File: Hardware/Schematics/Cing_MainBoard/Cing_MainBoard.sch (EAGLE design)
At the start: 116 parts, among them IC1 L293D, IC3 FT232RL, Q1 16mhz, Q2 BSS138, Q3 BSS138, Q4 BSS138, Q5 BSS138, U2 BMP180, U3 MPU-6050MPU6050

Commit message: commit
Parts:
- removed R8, R9: 1k, rcl:R-EU_R1206
- removed U$8: BATTERY_18650-HOLDER, Cing Library:BATTERY_18650-HOLDER
- added BT1: (no value), Cing Library:BATTERY-AA_KIT
- added IC2, IC4: Attiny85, Cing Library:TINY85-20SU
- added LED2: Empty, led:LEDSMT1206
- added M1: ELECTRET_MICROPHON-F6035AP, microphon:ELECTRET_MICROPHON-F6035AP
- added Q6: BSS138, Cing Library:BSS138
- added R42, R44, R45: 10k, rcl:R-EU_R1206
- added R43: 100, rcl:R-EU_R1206
- added SP1: AL11P, buzzer:AL11P
- added YELLOW1: Full, led:LEDSMT1206
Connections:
- removed net N$3: R8.1, U$1.D1
- removed net N$6: R9.1, U$1.D0
- new net N$21: IC2.PB1/PCINT1/AIN1/OC0B/INT0/MISO, LED2.A
- new net N$28: Q6.D, SP1.1
- new net N$30: LED2.C, R43.1, YELLOW1.C
- new net N$37: IC2.PB4/PCINT4/ADC2, YELLOW1.A
- new net N$38: IC4.PB1/PCINT1/AIN1/OC0B/INT0/MISO, Q6.G, R45.1
- new net VOLTAGE_SENSE: IC2.PB3/PCINT3/CLKI/ADC3, R42.2, R44.1
- net +3V3: now also IC2.VCC, IC4.VCC, SP1.2
- net GND: now also BT1.-, IC2.GND, IC4.GND, Q6.S, R43.2, R44.2, R45.2; no longer U$8.-, U$8.-1, U$8.-2
- net IRFU: now also BT1.+, R42.1; no longer U$8.+, U$8.+1, U$8.+2
- net RXD: now also U$1.D0; no longer R9.2
- net SCL: now also IC2.PB2/PCINT2/SCK/ADC1/T0, IC4.PB2/PCINT2/SCK/ADC1/T0
- net SDA: now also IC2.PB0/PCINT0/AIN0/OC0A/MOSI, IC4.PB0/PCINT0/AIN0/OC0A/MOSI
- net TXD: now also U$1.D1; no longer R8.2

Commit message: commit
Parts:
- added JP1: (no value), pinhead:PINHD-1X3
- added LED10, LED11, LED4, LED9: WS2812B3535, adafruit:WS2812B3535
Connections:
- new net N$41: JP1.2, LED11.DO, LED8.DO
- net +3V3: now also JP1.1, LED10.VDD, LED11.VDD, LED4.VDD, LED9.VDD
- net GND: now also JP1.3, LED10.GND, LED11.GND, LED4.GND, LED9.GND
- net N$1: now also LED10.DO, LED9.DI
- net N$11: now also LED11.DI, LED4.DO
- net N$12: now also LED10.DI
- net N$2: now also LED4.DI, LED9.DO

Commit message: commit
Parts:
- removed D2: CGRM4007-G, diode:CGRM4007-G
- removed LED2: Empty, led:LEDSMT1206
- removed R42, R44: 10k, rcl:R-EU_R1206
- removed R43: 100, rcl:R-EU_R1206
- removed U$21: DC-DC-STEP-UP-MT3608, Cing Library:DC-DC-STEP-UP-MT3608
- removed U2: BMP180, Cing Library:BMP180
- removed YELLOW1: Full, led:LEDSMT1206
- added 1, 8205: 8205, FS8205A:DMN3024LSD
- added C14, C15: 22uf, rcl:C-EUC1206
- added C16: 100n, rcl:C-EUC1206
- added C17: (no value), rcl:CPOL-EUE3.5-8
- added D3: (no value), adafruit:DIODESMA
- added IC5: BME280, bosch-bme280:BME280
- added L1: DR125, inductors:DR125
- added L2: DR127, inductors:DR127
- added R46, R47, R8: 1k, rcl:R-EU_R1206
- added R48: 100, rcl:R-EU_R1206
- added R49: 7k5, rcl:R-EU_R1206
- added R9: 12k, rcl:R-EU_R1206
- added SJ1: (no value), jumper:SJW
- added SJ2: (no value), jumper:SJ
- added U$13: ADS1015IDGT, bt_adc:ADS1015IDGT
- added U$5: MT3608SOT23-6, MT3608:MT3608SOT23-6
- added U$8: DW01, DW01:DW01
- added U$9: LM1117, Cing Library:LM1117
- D1: value CGRM4007-G -> (none); device diode:CGRM4007-G -> adafruit:DIODESMA
- IC2: value Attiny85 -> LM2576S; device Cing Library:TINY85-20SU -> lm2576:LM2576S
- R4: value 1k2 -> 1k
- R41: value 10k -> 2; device rcl:R-EU_R1206 -> rcl:R-EU_R2512
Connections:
- removed net N$23: D1.A, D2.C, R41.1, TP4056.BAT
- removed net N$30: LED2.C, R43.1, YELLOW1.C
- removed net N$37: IC2.PB4/PCINT4/ADC2, YELLOW1.A
- removed net VOLTAGE_SENSE: IC2.PB3/PCINT3/CLKI/ADC3, R42.2, R44.1
- new net BAT-: 1A.S, 8205A.S, BT1.-, C16.2, U$7.-, U$8.GND
- new net CUR-SENSE: R22.1, R41.2, SW5.CH1B, SW5.CH2B, U$13.AIN2
- new net N$3: 1A.D, 1B.D
- new net N$35: R46.1, R49.2, R9.2, U$5.FB
- new net N$44: D3.A, L1.2, U$5.SW
- new net N$46: C14.1, D3.C, R49.1, R9.1, SJ1.1
- new net N$47: 8205A.D, 8205B.D
- new net N$48: 1A.G, 8205A.G, U$8.0D
- new net N$49: 1B.G, 8205B.G, U$8.0C
- new net N$50: C16.1, R48.1, U$8.VCC
- new net N$54: R47.1, U$8.CS
- new net N$6: R4.2, R8.1
- new net VCC_SERVO: C17.+, IC2.FB, JP2.2, JP3.2, JP4.2, L2.2
- new net VDD: U$13.VDD, U$9.OUT, U$9.VO
- net +3V3: now also IC5.CSB, IC5.VDD, IC5.VDDIO; no longer IC2.VCC, U2.VDD, U2.VDDIO
- net BAT+: now also C15.1, L1.1, R41.1, R48.2, U$13.AIN0, U$13.AIN3, U$5.EN, U$5.IN, U$9.VI; no longer R22.1, SW5.CH1B, SW5.CH2B, U$21.IN+
- net GND: now also 1B.S, 8205B.S, C14.2, C15.2, C17.-, D1.A, IC5.GND, IC5.SDO, R46.2, R47.2, R8.2, U$13.ADDR, U$13.AIN1, U$13.GND, U$5.GND, U$9.GND; no longer BT1.-, D2.A, R4.2, R43.2, R44.2, U$21.IN-, U$21.OUT-, U$7.-, U2.GND
- net IRFU: now also SJ2.1; no longer D1.C, R41.2, R42.1
- net N$21: now also D1.C, IC2.OUT, L2.1; no longer IC2.PB1/PCINT1/AIN1/OC0B/INT0/MISO, LED2.A
- net N$26: now also SJ2.2, TP4056.BAT
- net SCL: now also IC5.SCK, U$13.SCL; no longer IC2.PB2/PCINT2/SCK/ADC1/T0, U2.SCL
- net SDA: now also IC5.SDI, U$13.SDA; no longer IC2.PB0/PCINT0/AIN0/OC0A/MOSI, U2.SDA
- net VCC_MOT: now also IC2.VIN, SJ1.2; no longer JP2.2, JP3.2, JP4.2, U$21.OUT+
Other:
- moved on the sheet: BT1, C10, C4, C5, C9, D1, R22, R3, SW1, SW5, TP4056, U$6

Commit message: commit
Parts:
- removed IC4: Attiny85, Cing Library:TINY85-20SU
- removed M1: ELECTRET_MICROPHON-F6035AP, microphon:ELECTRET_MICROPHON-F6035AP
- removed Q6: BSS138, Cing Library:BSS138
- removed R45: 10k, rcl:R-EU_R1206
- removed SP1: AL11P, buzzer:AL11P
- added U$14: RANGING-SENSOR-VL53L0X, diy-modules:RANGING-SENSOR-VL53L0X
- U$16: value 3.3V -> BAT+
- U$9: value LM1117 -> LM1117-5V
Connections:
- removed net N$28: Q6.D, SP1.1
- removed net N$38: IC4.PB1/PCINT1/AIN1/OC0B/INT0/MISO, Q6.G, R45.1
- net +3V3: no longer IC4.VCC, SP1.2, U$16.LEGO
- net BAT+: now also U$16.LEGO
- net GND: now also U$14.GND; no longer IC4.GND, Q6.S, R45.2
- net SCL: now also U$14.SCL; no longer IC4.PB2/PCINT2/SCK/ADC1/T0
- net SDA: now also U$14.SDA; no longer IC4.PB0/PCINT0/AIN0/OC0A/MOSI
- net VDD: now also U$14.VIN

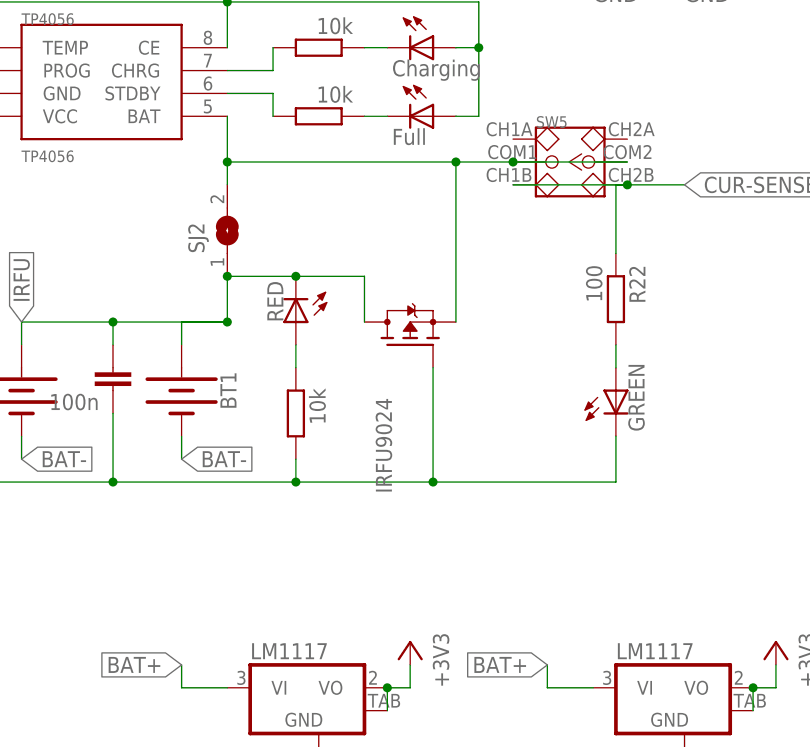
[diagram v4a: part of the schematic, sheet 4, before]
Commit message: Adding better P-fet
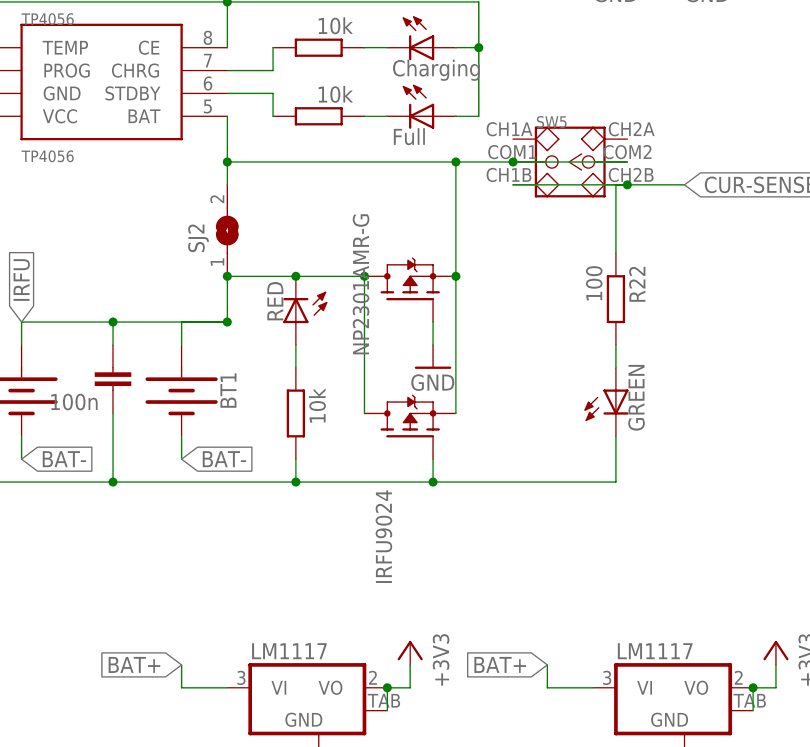
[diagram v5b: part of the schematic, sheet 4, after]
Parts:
- added Q7: NP2301AMR-G, transistor-fet:BSA223SP
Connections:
- net GND: now also Q7.G
- net IRFU: now also Q7.D
- net N$26: now also Q7.S
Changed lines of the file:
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@@
 <part name="U$14" library="diy-modules" deviceset="RANGING-SENSOR-VL53L0X" device=""/>
 <part name="GND48" library="supply1" library_urn="urn:adsk.eagle:library:371" deviceset="GND" device=""/>
+<part name="Q7" library="transistor-fet" library_urn="urn:adsk.eagle:library:396" deviceset="BSA223SP" device="" package3d_urn="urn:adsk.eagle:package:28542/1" value="NP2301AMR-G"/>
+<part name="GND49" library="supply1" library_urn="urn:adsk.eagle:library:371" deviceset="GND" device=""/>
 </parts>
 <sheets>
@@
 <attribute name="VALUE" x="251.46" y="53.34" size="1.778" layer="96" rot="MR90"/>
 </instance>
-<instance part="IRFU9024" gate="G$1" x="208.28" y="91.44" smashed="yes" rot="MR90"/>
+<instance part="IRFU9024" gate="G$1" x="208.28" y="81.28" smashed="yes" rot="MR90"/>
 <instance part="U$7" gate="G$1" x="165.1" y="86.36" smashed="yes" rot="R270"/>
 <instance part="TP4056" gate="G$1" x="165.1" y="127" smashed="yes">
@@
 <attribute name="NAME" x="63.5" y="104.14" size="1.27" layer="95" rot="R90"/>
 <attribute name="VALUE" x="69.85" y="104.14" size="1.27" layer="96" rot="R90"/>
+</instance>
+<instance part="Q7" gate="G$1" x="208.28" y="96.52" smashed="yes" rot="MR90">
+<attribute name="VALUE" x="201.93" y="90.17" size="1.778" layer="96" rot="MR90"/>
+</instance>
+<instance part="GND49" gate="1" x="210.82" y="88.9" smashed="yes">
+<attribute name="VALUE" x="208.28" y="86.36" size="1.778" layer="96"/>
 </instance>
 </instances>
@@
 <wire x1="175.26" y1="76.2" x2="195.58" y2="76.2" width="0.1524" layer="91"/>
 <wire x1="195.58" y1="76.2" x2="210.82" y2="76.2" width="0.1524" layer="91"/>
-<wire x1="210.82" y1="88.9" x2="210.82" y2="76.2" width="0.1524" layer="91"/>
+<wire x1="210.82" y1="78.74" x2="210.82" y2="76.2" width="0.1524" layer="91"/>
 <junction x="210.82" y="76.2"/>
 <pinref part="C1" gate="G$1" pin="2"/>
@@
 <junction x="66.04" y="104.14"/>
 </segment>
+<segment>
+<pinref part="Q7" gate="G$1" pin="G"/>
+<pinref part="GND49" gate="1" pin="GND"/>
+<wire x1="210.82" y1="91.44" x2="210.82" y2="93.98" width="0.1524" layer="91"/>
+</segment>
 </net>
 <net name="IRFU" class="0">
@@
 <wire x1="187.96" y1="99.06" x2="187.96" y2="93.98" width="0.1524" layer="91"/>
 <wire x1="195.58" y1="99.06" x2="187.96" y2="99.06" width="0.1524" layer="91"/>
-<wire x1="203.2" y1="93.98" x2="203.2" y2="99.06" width="0.1524" layer="91"/>
+<wire x1="203.2" y1="83.82" x2="203.2" y2="99.06" width="0.1524" layer="91"/>
 <wire x1="203.2" y1="99.06" x2="195.58" y2="99.06" width="0.1524" layer="91"/>
 <pinref part="BT1" gate="G$1" pin="+"/>
@@
 <pinref part="SJ2" gate="1" pin="1"/>
 <junction x="187.96" y="99.06"/>
+<pinref part="Q7" gate="G$1" pin="D"/>
+<junction x="203.2" y="99.06"/>
 </segment>
 </net>
@@
 <wire x1="219.71" y1="111.76" x2="213.36" y2="111.76" width="0.1524" layer="91"/>
 <junction x="219.71" y="111.76"/>
-<wire x1="213.36" y1="93.98" x2="213.36" y2="111.76" width="0.1524" layer="91"/>
+<wire x1="213.36" y1="83.82" x2="213.36" y2="99.06" width="0.1524" layer="91"/>
 <pinref part="IRFU9024" gate="G$1" pin="S"/>
 <pinref part="TP4056" gate="G$1" pin="BAT"/>
+<wire x1="213.36" y1="99.06" x2="213.36" y2="111.76" width="0.1524" layer="91"/>
 <wire x1="187.96" y1="116.84" x2="187.96" y2="111.76" width="0.1524" layer="91"/>
 <wire x1="187.96" y1="111.76" x2="213.36" y2="111.76" width="0.1524" layer="91"/>
@@
 <wire x1="187.96" y1="111.76" x2="187.96" y2="109.22" width="0.1524" layer="91"/>
 <junction x="187.96" y="111.76"/>
-</segment>
-</net>
+<pinref part="Q7" gate="G$1" pin="S"/>
+<junction x="213.36" y="99.06"/>
+</segment>
+</net>

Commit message: commit
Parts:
- added Q6: NP2301AMR-G, transistor-fet:BSA223SP
- added U$15: (no value), diy-modules:COMPASS-HMC5883L
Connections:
- net +3V3: now also U$15.VCC
- net GND: now also Q6.G, U$15.GND
- net IRFU: now also Q6.D
- net N$26: now also Q6.S
- net SCL: now also U$15.SCL
- net SDA: now also U$15.SDA

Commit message: commit
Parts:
- renumbered JP1 to WS2812
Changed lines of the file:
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@@
 <part name="GND52" library="supply1" library_urn="urn:adsk.eagle:library:371" deviceset="GND" device=""/>
 <part name="GND53" library="supply1" library_urn="urn:adsk.eagle:library:371" deviceset="GND" device=""/>
-<part name="JP1" library="pinhead" library_urn="urn:adsk.eagle:library:325" deviceset="PINHD-1X3" device="" package3d_urn="urn:adsk.eagle:package:22458/2"/>
+<part name="WS2812" library="pinhead" library_urn="urn:adsk.eagle:library:325" deviceset="PINHD-1X3" device="" package3d_urn="urn:adsk.eagle:package:22458/2"/>
 <part name="GND54" library="supply1" library_urn="urn:adsk.eagle:library:371" deviceset="GND" device=""/>
 <part name="+3V27" library="supply1" library_urn="urn:adsk.eagle:library:371" deviceset="+3V3" device=""/>
@@
 <attribute name="VALUE" x="43.18" y="96.52" size="1.778" layer="96" rot="MR180"/>
 </instance>
-<instance part="JP1" gate="A" x="142.24" y="66.04" smashed="yes">
+<instance part="WS2812" gate="A" x="142.24" y="66.04" smashed="yes">
 <attribute name="NAME" x="143.51" y="71.755" size="1.778" layer="95"/>
 <attribute name="VALUE" x="135.89" y="58.42" size="1.778" layer="96"/>
@@
 </segment>
 <segment>
-<pinref part="JP1" gate="A" pin="3"/>
+<pinref part="WS2812" gate="A" pin="3"/>
 <wire x1="139.7" y1="63.5" x2="137.16" y2="63.5" width="0.1524" layer="91"/>
 <pinref part="GND54" gate="1" pin="GND"/>
@@
 </segment>
 <segment>
-<pinref part="JP1" gate="A" pin="1"/>
+<pinref part="WS2812" gate="A" pin="1"/>
 <wire x1="139.7" y1="68.58" x2="137.16" y2="68.58" width="0.1524" layer="91"/>
 <pinref part="+3V27" gate="G$1" pin="+3V3"/>
@@
 <wire x1="134.62" y1="66.04" x2="139.7" y2="66.04" width="0.1524" layer="91"/>
 <junction x="134.62" y="66.04"/>
-<pinref part="JP1" gate="A" pin="2"/>
+<pinref part="WS2812" gate="A" pin="2"/>
 </segment>
 </net>

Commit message: commit
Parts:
- added C18, C19, C20: 100n, rcl:C-EUC1206
- added JP1, JP10, JP11, JP12, JP13, JP14, JP15, JP16, JP17, JP18, JP19, JP20, JP21, JP22, JP6, JP7, JP8, JP9: (no value), pinhead:PINHD-1X1
- added R42, R43: 10k, rcl:R-EU_R1206
- added SW7: (no value), Cing Library:USB_SWITCH
- added U$21: SX1509, Cing Library:SX1509
- added U$23: WIRELESS-BLUETOOTH-HC-05, Cing Library:WIRELESS-BLUETOOTH-HC-05
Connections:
- new net A0H: SW7.COM1, U$2.A0
- new net N$23: R42.2, U$21.NINT
- new net N$28: R43.1, U$21.NRESET
- new net N$30: JP1.1, U$21.I/O[6]
- new net N$37: JP6.1, U$21.I/O[5]
- new net N$38: JP7.1, U$21.I/O[4]
- new net N$51: JP8.1, U$21.I/O[2]
- new net N$52: JP9.1, U$21.I/O[3]
- new net N$53: JP10.1, U$21.I/O[1]
- new net N$55: JP11.1, U$21.I/O[0]
- new net N$56: JP12.1, U$21.I/O[14]
- new net N$57: JP13.1, U$21.I/O[13]
- new net N$58: JP14.1, U$21.I/O[12]
- new net N$59: JP15.1, U$21.I/O[10]
- new net N$60: JP16.1, U$21.I/O[9]
- new net N$61: JP17.1, U$21.I/O[8]
- new net N$62: JP18.1, U$21.I/O[7]
- new net N$63: JP19.1, U$21.I/O[11]
- new net N$64: JP20.1, U$21.I/O[15]
- new net N$65: C18.2, IC3._RTS
- new net N$66: R23.P$2, R29.1, SW7.CH1A
- net +3V3: now also C19.1, C20.1, JP21.1, JP22.1, R42.1, R43.2, U$21.VCC1, U$21.VCC2, U$21.VDDM
- net A0: now also SW7.CH1B; no longer U$2.A0
- net A6: no longer R23.P$2, R29.1
- net BAT+: now also U$23.+5V
- net D2: now also U$23.TX
- net D5: now also U$23.RX
- net GND: now also C19.2, C20.2, U$21.ADDR0, U$21.ADDR1, U$21.GND1, U$21.GND2, U$23.GND
- net RESET: now also C18.1
- net SCL: now also U$21.SCL
- net SDA: now also U$21.SDA
